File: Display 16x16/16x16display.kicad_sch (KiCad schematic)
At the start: 42 parts, among them J1 86093967113745ELF, U1 7130LA55PDGI, U10 SN74AHCT240DWR, U11 74AHC244, U12 74HC138, U2 GAL16V8, U3 GAL16V8, U4 74ahc1G14dckr, U5 74HCT238, U6 74HCT238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

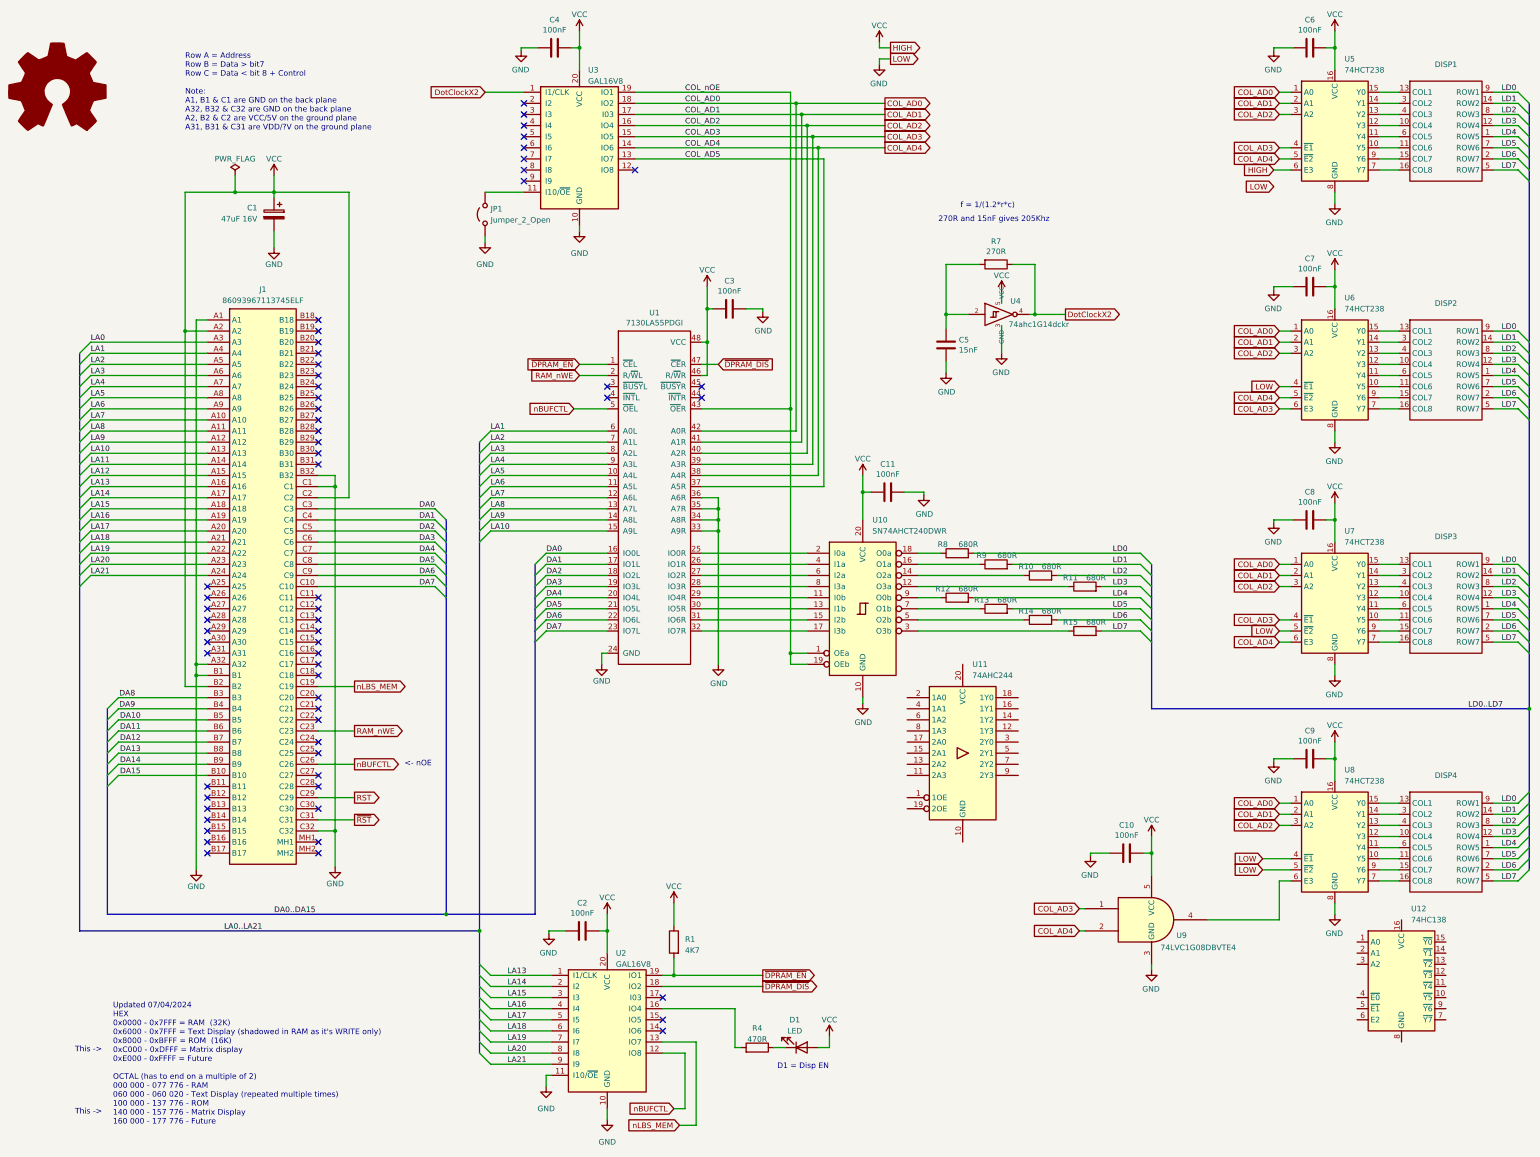
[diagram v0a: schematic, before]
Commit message: Update with correct chips (no change to PCB)
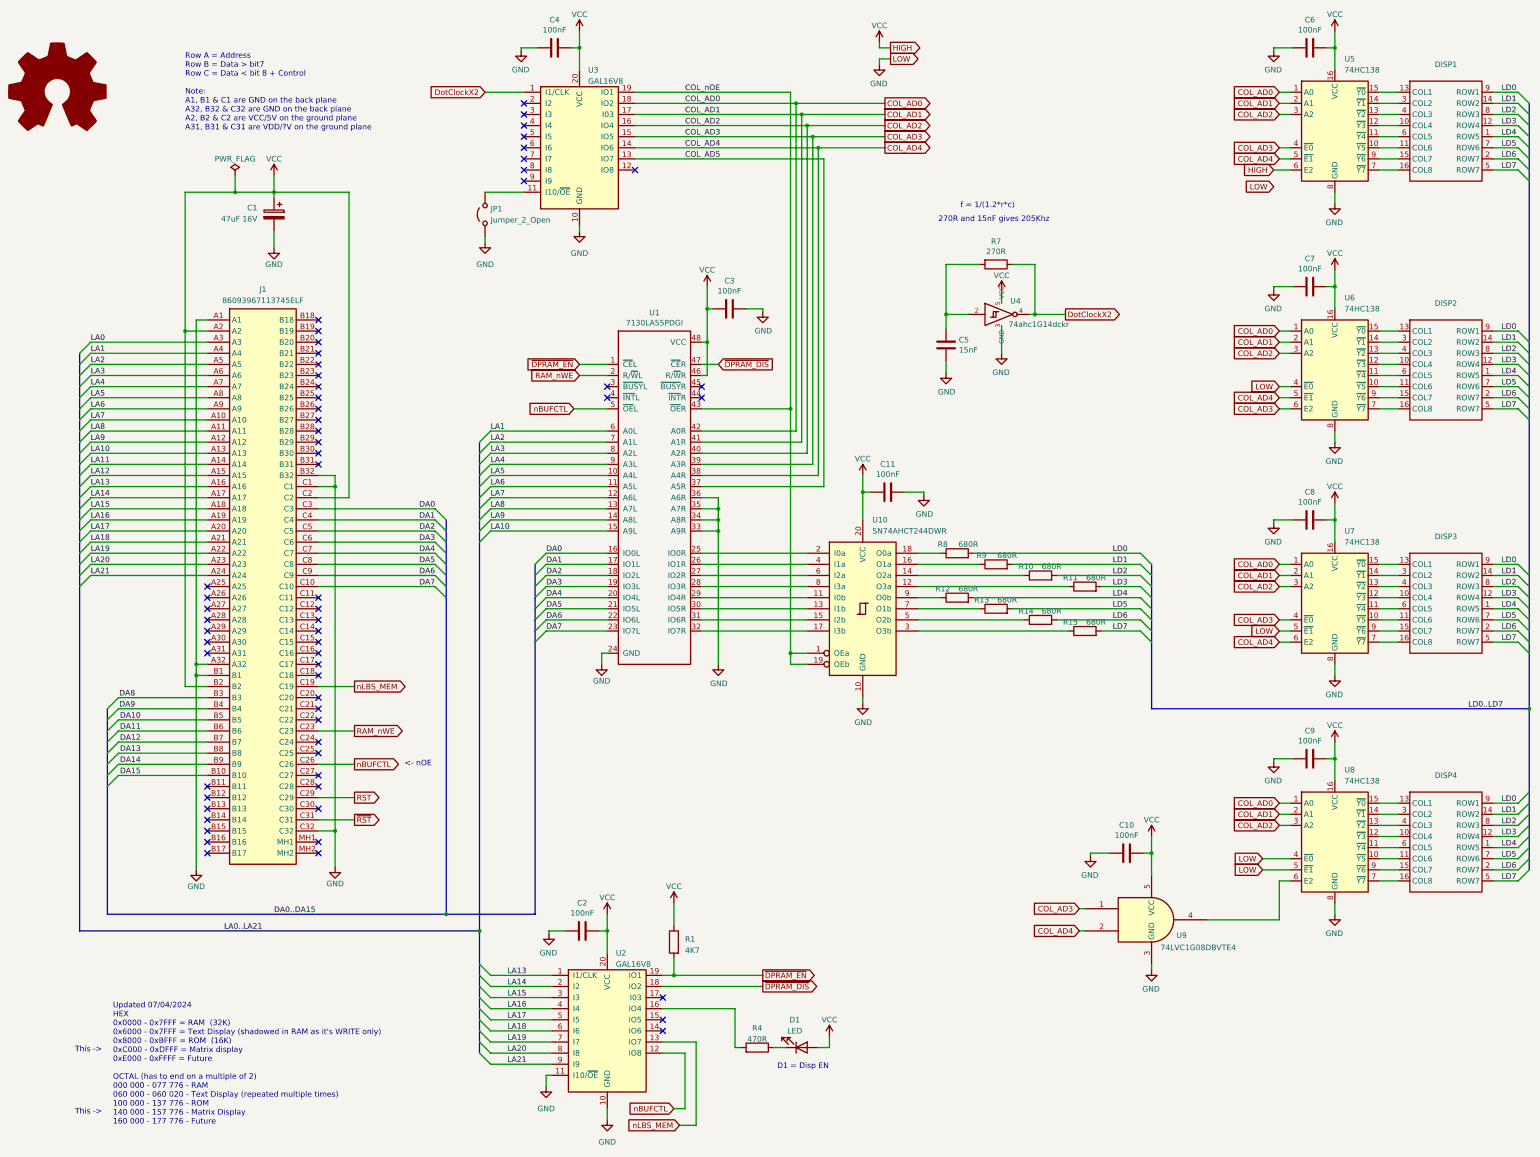
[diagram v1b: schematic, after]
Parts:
- removed U10: SN74AHCT240DWR, Package_SO:SOIC-20W_7.5x12.8mm_P1.27mm, symbol 74xx:74LS240
- removed U11: 74AHC244, symbol 74xx:74AHC244
- removed U5, U6, U7, U8: 74HCT238, Package_SO:SO-16_3.9x9.9mm_P1.27mm, symbol 74xx:74HCT238
- added U10: SN74AHCT244DWR, Package_SO:SOIC-20W_7.5x12.8mm_P1.27mm, symbol 74xx:74LS244
- added U6, U7, U8: 74HC138, Package_SO:SO-16_3.9x9.9mm_P1.27mm, symbol 74xx:74HC138
- U5: renamed from U12; footprint (none) -> Package_SO:SO-16_3.9x9.9mm_P1.27mm
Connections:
- net COL_AD0: now also U5.1 (A0), U6.1 (A0), U7.1 (A0), U8.1 (A0)
- net COL_AD1: now also U5.2 (A1), U6.2 (A1), U7.2 (A1), U8.2 (A1)
- net COL_AD2: now also U5.3 (A2), U6.3 (A2), U7.3 (A2), U8.3 (A2)
- net COL_AD3: now also U5.4 (~{E0}), U6.6 (E2), U7.4 (~{E0})
- net COL_AD4: now also U5.5 (~{E1}), U6.5 (~{E1}), U7.6 (E2)
- net COL_nOE: now also U10.1 (OEa), U10.19 (OEb)
- net GND: now also U5.8 (GND), U10.10 (GND), U6.4 (~{E0}), U6.8 (GND), U7.5 (~{E1}), U7.8 (GND), U8.4 (~{E0}), U8.5 (~{E1}), U8.8 (GND)
- net VCC: now also U5.16 (VCC), U5.6 (E2), U10.20 (VCC), U6.16 (VCC), U7.16 (VCC), U8.16 (VCC)
- net at R10.1: now also U10.14 (O2a)
- net at R14.1: now also U10.5 (O2b)
- net at U1.25 (IO0R): now also U10.2 (I0a)
- net at U1.26 (IO1R): now also U10.4 (I1a)
- net at U1.27 (IO2R): now also U10.6 (I2a)
- net at U1.28 (IO3R): now also U10.8 (I3a)
- net at U1.29 (IO4R): now also U10.11 (I0b)
- net at U1.30 (IO5R): now also U10.13 (I1b)
- net at U1.31 (IO6R): now also U10.15 (I2b)
- net at U1.32 (IO7R): now also U10.17 (I3b)
- net at R12.1: now also U10.9 (O0b)
- net at DISP1.11 (COL6): now also U5.10 (~{Y5})
- net at DISP1.6 (COL5): now also U5.11 (~{Y4})
- net at DISP1.10 (COL4): now also U5.12 (~{Y3})
- net at DISP1.4 (COL3): now also U5.13 (~{Y2})
- net at DISP1.3 (COL2): now also U5.14 (~{Y1})
- net at DISP1.13 (COL1): now also U5.15 (~{Y0})
- net at DISP1.16 (COL8): now also U5.7 (~{Y7})
- net at DISP1.15 (COL7): now also U5.9 (~{Y6})
- net at R15.1: now also U10.3 (O3b)
- net at DISP2.10 (COL4): now also U6.12 (~{Y3})
- net at DISP2.11 (COL6): now also U6.10 (~{Y5})
- net at DISP2.13 (COL1): now also U6.15 (~{Y0})
- net at DISP2.15 (COL7): now also U6.9 (~{Y6})
- net at DISP2.16 (COL8): now also U6.7 (~{Y7})
- net at DISP2.3 (COL2): now also U6.14 (~{Y1})
- net at DISP2.4 (COL3): now also U6.13 (~{Y2})
- net at DISP2.6 (COL5): now also U6.11 (~{Y4})
- net at U9.4: now also U8.6 (E2)
- net at DISP4.10 (COL4): now also U8.12 (~{Y3})
- net at DISP4.11 (COL6): now also U8.10 (~{Y5})
- net at DISP4.13 (COL1): now also U8.15 (~{Y0})
- net at DISP4.15 (COL7): now also U8.9 (~{Y6})
- net at DISP4.16 (COL8): now also U8.7 (~{Y7})
- net at DISP4.3 (COL2): now also U8.14 (~{Y1})
- net at DISP4.4 (COL3): now also U8.13 (~{Y2})
- net at DISP4.6 (COL5): now also U8.11 (~{Y4})
- net at R11.1: now also U10.12 (O3a)
- net at R9.1: now also U10.16 (O1a)
- net at R8.1: now also U10.18 (O0a)
- net at R13.1: now also U10.7 (O1b)
- net at DISP3.10 (COL4): now also U7.12 (~{Y3})
- net at DISP3.11 (COL6): now also U7.10 (~{Y5})
- net at DISP3.13 (COL1): now also U7.15 (~{Y0})
- net at DISP3.15 (COL7): now also U7.9 (~{Y6})
- net at DISP3.16 (COL8): now also U7.7 (~{Y7})
- net at DISP3.3 (COL2): now also U7.14 (~{Y1})
- net at DISP3.4 (COL3): now also U7.13 (~{Y2})
- net at DISP3.6 (COL5): now also U7.11 (~{Y4})
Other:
- moved on the sheet: U5
